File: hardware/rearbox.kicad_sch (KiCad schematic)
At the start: 0 parts

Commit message: Add components
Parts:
- added C1, C4, C5, C6, C7, C8: 100n, Capacitor_SMD:C_0603_1608Metric, symbol Device:C_Small
- added C2, C3: 10p, Capacitor_SMD:C_0603_1608Metric, symbol Device:C_Small
- added C?: 1u, Capacitor_SMD:C_0402_1005Metric_Pad0.74x0.62mm_HandSolder, symbol Device:C_Small
- added C?: 100n, Capacitor_SMD:C_0402_1005Metric_Pad0.74x0.62mm_HandSolder, symbol Device:C_Small
- added J1: Conn_01x06, Connector_PinHeader_2.54mm:PinHeader_1x06_P2.54mm_Vertical, symbol Connector_Generic:Conn_01x06
- added R1: 1k, Resistor_SMD:R_0402_1005Metric, symbol Device:R_Small
- added R2: 10k, Resistor_SMD:R_0402_1005Metric, symbol Device:R_Small
- added SW1: Tactswitch, Button_Switch_SMD:SW_SPST_B3U-1000P, symbol Switch:SW_Push
- added U1: STM32G473RCTx, Package_QFP:LQFP-64_10x10mm_P0.5mm, symbol MCU_ST_STM32G4:STM32G473RCTx
- added Y1: ABM8G-48.000MHZ, Crystal:Crystal_SMD_Abracon_ABM8G-4Pin_3.2x2.5mm, symbol Device:Crystal_GND24_Small
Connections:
- new net: R1.2, SW1.2
- new net +3.3VA: C?.1, C?.1, U1.29 (VDDA)
- new net +3V3: C1.1, C4.1, C6.1, C7.1, C8.1, J1.1 (Pin_1), R2.1, U1.1 (VBAT), U1.16 (VDD), U1.32 (VDD), U1.48 (VDD), U1.64 (VDD)
- new net ANALOG_INPUT1: U1.34 (PB12)
- new net ANALOG_INPUT2: U1.35 (PB13)
- new net ANALOG_INPUT3: U1.36 (PB14)
- new net ANALOG_INPUT4: U1.37 (PB15)
- new net ASSI_LED_BLUE: U1.3 (PC14)
- new net ASSI_LED_BUZZER: U1.4 (PC15)
- new net ASSI_LED_GREEN: U1.2 (PC13)
- new net ASSI_LED_RED: U1.54 (PC12)
- new net BRAKE_LIGHT: U1.24 (PB0)
- new net CAN2_RX: U1.61 (PB8)
- new net CAN2_TX: U1.62 (PB9)
- new net CAN_RX: U1.58 (PB5)
- new net CAN_TX: U1.59 (PB6)
- new net FAN_L: U1.25 (PB1)
- new net FAN_R: U1.26 (PB2)
- new net GND: C1.2, C2.2, C3.2, C4.2, C5.2, C6.2, C7.2, C8.2, C?.2, C?.2, J1.3 (Pin_3), SW1.1, U1.15 (VSS), U1.27 (VSSA), U1.31 (VSS), U1.47 (VSS), U1.63 (VSS), Y1.2, Y1.4
- new net HSE_IN: C2.1, U1.5 (PF0), Y1.1
- new net HSE_OUT: C3.1, U1.6 (PF1), Y1.3
- new net I^{2}C_SCL: U1.40 (PC8)
- new net I^{2}C_SDA: U1.41 (PC9)
- new net LED_CAN: U1.42 (PA8)
- new net LED_ERROR: U1.43 (PA9)
- new net LED_FUSE1: U1.44 (PA10)
- new net LED_FUSE2: U1.51 (PA15)
- new net LED_FUSE3: U1.60 (PB7)
- new net LED_FUSE4: U1.33 (PB11)
- new net MONO_TEMPERATURE: U1.10 (PC2)
- new net NRST: C5.1, J1.5 (Pin_5), R1.1, R2.2, U1.7 (PG10)
- new net PUMP_L: U1.56 (PB3)
- new net PUMP_R: U1.57 (PB4)
- new net RTDS_IN: U1.30 (PB10)
- new net SPI_MISO: U1.20 (PA6)
- new net SPI_MOSI: U1.21 (PA7)
- new net SPI_SCLK: U1.19 (PA5)
- new net SUSPENSION_POT1: U1.12 (PA0)
- new net SUSPENSION_POT2: U1.13 (PA1)
- new net SWCLK: J1.2 (Pin_2), U1.50 (PA14)
- new net SWDIO: J1.4 (Pin_4), U1.49 (PA13)
- new net UART_RX: U1.53 (PC11)
- new net UART_TX: U1.52 (PC10)
- new net USB_D+: U1.46 (PA12)
- new net USB_D-: U1.45 (PA11)
- new net WATER_PRESSURE1: U1.38 (PC6)
- new net WATER_PRESSURE2: U1.39 (PC7)
- new net WATER_TEMPERATURE1: U1.8 (PC0)
- new net WATER_TEMPERATURE2: U1.9 (PC1)
- new net ~{SPI_SS1}: U1.22 (PC4)
- new net ~{SPI_SS2}: U1.17 (PA3)
- new net ~{SPI_SS3}: U1.18 (PA4)
- no-connect marks 0 -> 2
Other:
- added sheet ASSI (assi.kicad_sch)
- added sheet Analog Inputs (analog_inputs.kicad_sch)
- added sheet Autosport (autosport.kicad_sch)
- added sheet Brake Light (brake_light.kicad_sch)
- added sheet CAN Transceivers (can_transceivers.kicad_sch)
- added sheet Fans (fans.kicad_sch)
- added sheet LEDs (leds.kicad_sch)
- added sheet Power Supply (power_supply.kicad_sch)
- added sheet Pumps (pumps.kicad_sch)
- added sheet RTDS (ready_to_drive_sound.kicad_sch)
- added sheet Safety Inputs (safety_inputs.kicad_sch)
- added sheet Suspension Potentiometers (suspension_potentiometers.kicad_sch)
- added sheet Temperature Sensors (temperature_sensors.kicad_sch)
- added sheet USB (usb.kicad_sch)
- added sheet Water Pressure Sensors (water_pressure_sensors.kicad_sch)
- note added: "GND"
- note added: "NRST"
- note added: "SWCLK"
- note added: "SWDIO"
- note added: "SWO"
- note added: "VDD"
- company: Author: I.Kajdan -> Author: I. Kajdan

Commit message: Add the Cube project
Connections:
- net ASSI_LED_RED is gone; now on net SPI_MOSI: U1.54 (PC12)
- net RTDS_IN is gone; now on net PUMP_R: U1.30 (PB10)
- net ~{SPI_SS1} is gone; now on net ANALOG_INPUT3: U1.22 (PC4)
- net ANALOG_INPUT1: now also U1.20 (PA6); no longer U1.34 (PB12)
- net ANALOG_INPUT2: now also U1.21 (PA7); no longer U1.35 (PB13)
- net ANALOG_INPUT3: no longer U1.36 (PB14)
- net ANALOG_INPUT4: now also U1.23 (PC5); no longer U1.37 (PB15)
- net BRAKE_LIGHT: now also U1.25 (PB1); no longer U1.24 (PB0)
- net CAN2_RX: now also U1.58 (PB5); no longer U1.61 (PB8)
- net CAN2_TX: now also U1.59 (PB6); no longer U1.62 (PB9)
- net CAN_RX: now also U1.61 (PB8); no longer U1.58 (PB5)
- net CAN_TX: now also U1.62 (PB9); no longer U1.59 (PB6)
- net FAN_L: now also U1.37 (PB15); no longer U1.25 (PB1)
- net FAN_R: now also U1.36 (PB14); no longer U1.26 (PB2)
- net I^{2}C_SCL: now also U1.43 (PA9); no longer U1.40 (PC8)
- net I^{2}C_SDA: now also U1.42 (PA8); no longer U1.41 (PC9)
- net LED_CAN: no longer U1.42 (PA8)
- net LED_ERROR: no longer U1.43 (PA9)
- net PUMP_L: now also U1.35 (PB13); no longer U1.56 (PB3)
- net PUMP_R: no longer U1.57 (PB4)
- net SPI_MISO: now also U1.57 (PB4); no longer U1.20 (PA6)
- net SPI_MOSI: no longer U1.21 (PA7)
- net SPI_SCLK: now also U1.56 (PB3); no longer U1.19 (PA5)
- net SUSPENSION_POT1: now also U1.13 (PA1); no longer U1.12 (PA0)
- net SUSPENSION_POT2: now also U1.14 (PA2); no longer U1.13 (PA1)
- net WATER_PRESSURE1: now also U1.11 (PC3); no longer U1.38 (PC6)
- net WATER_PRESSURE2: now also U1.12 (PA0); no longer U1.39 (PC7)
- net +3V3 renamed +3.3V
- net ASSI_LED_BLUE renamed ASSI_LED_G
- net ASSI_LED_BUZZER renamed ASSI_LED_B
- net ASSI_LED_GREEN renamed ASSI_LED_R
- net LED_FUSE1: no longer names the net of U1.44 (PA10)
- net LED_FUSE2: no longer names the net of U1.51 (PA15)
- net LED_FUSE3: no longer names the net of U1.60 (PB7)
- net LED_FUSE4: no longer names the net of U1.33 (PB11)
- net ~{SPI_SS2} renamed ASSI_BUZZER
- net ~{SPI_SS3} renamed ANALOG_OFFSET1
- new net ANALOG_OFFSET2: U1.19 (PA5)
- new net BUZZER: U1.26 (PB2)
- new net RTDS: U1.24 (PB0)
- new net SAFETY_SCL: U1.40 (PC8)
- new net SAFETY_SDA: U1.41 (PC9)
- new net SAFETY_~{INT}: U1.39 (PC7)
- new net SAFETY_~{RESET}: U1.38 (PC6)
- no-connect marks 2 -> 8
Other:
- sheet LEDs renamed LEDs & Buzzer
- sheet ASSI ports: added IN_BUZZER, OUT_BUZZER; removed IN_BUZZ, OUT_BUZZ
- sheet Analog Inputs ports: added REF1, REF2; removed none
- sheet LEDs & Buzzer ports: added BUZZER, FUSE, SAFETY; removed FUSE1, FUSE2, FUSE3, FUSE4
- sheet Safety Inputs ports: added IN_WHEEL_FL, IN_WHEEL_FR, IN_WHEEL_RL, IN_WHEEL_RR, LED_CAN, LED_ERROR, LED_FUSE, LED_SAFETY, SCL, SDA, ~{INT}, ~{RESET}; removed IN_W_FL, IN_W_FR, IN_W_RL, IN_W_RR, OUT_ASMS, OUT_FW, OUT_HV, OUT_HVD, OUT_INV, OUT_RES, OUT_RFU1, OUT_RFU2, OUT_W_FL, OUT_W_FR, OUT_W_RL, OUT_W_RR
- sheet Suspension Potentiometers ports: added IN_L, IN_R, OUT_L, OUT_R; removed IN1, IN2, OUT1, OUT2
- moved on the sheet: U1

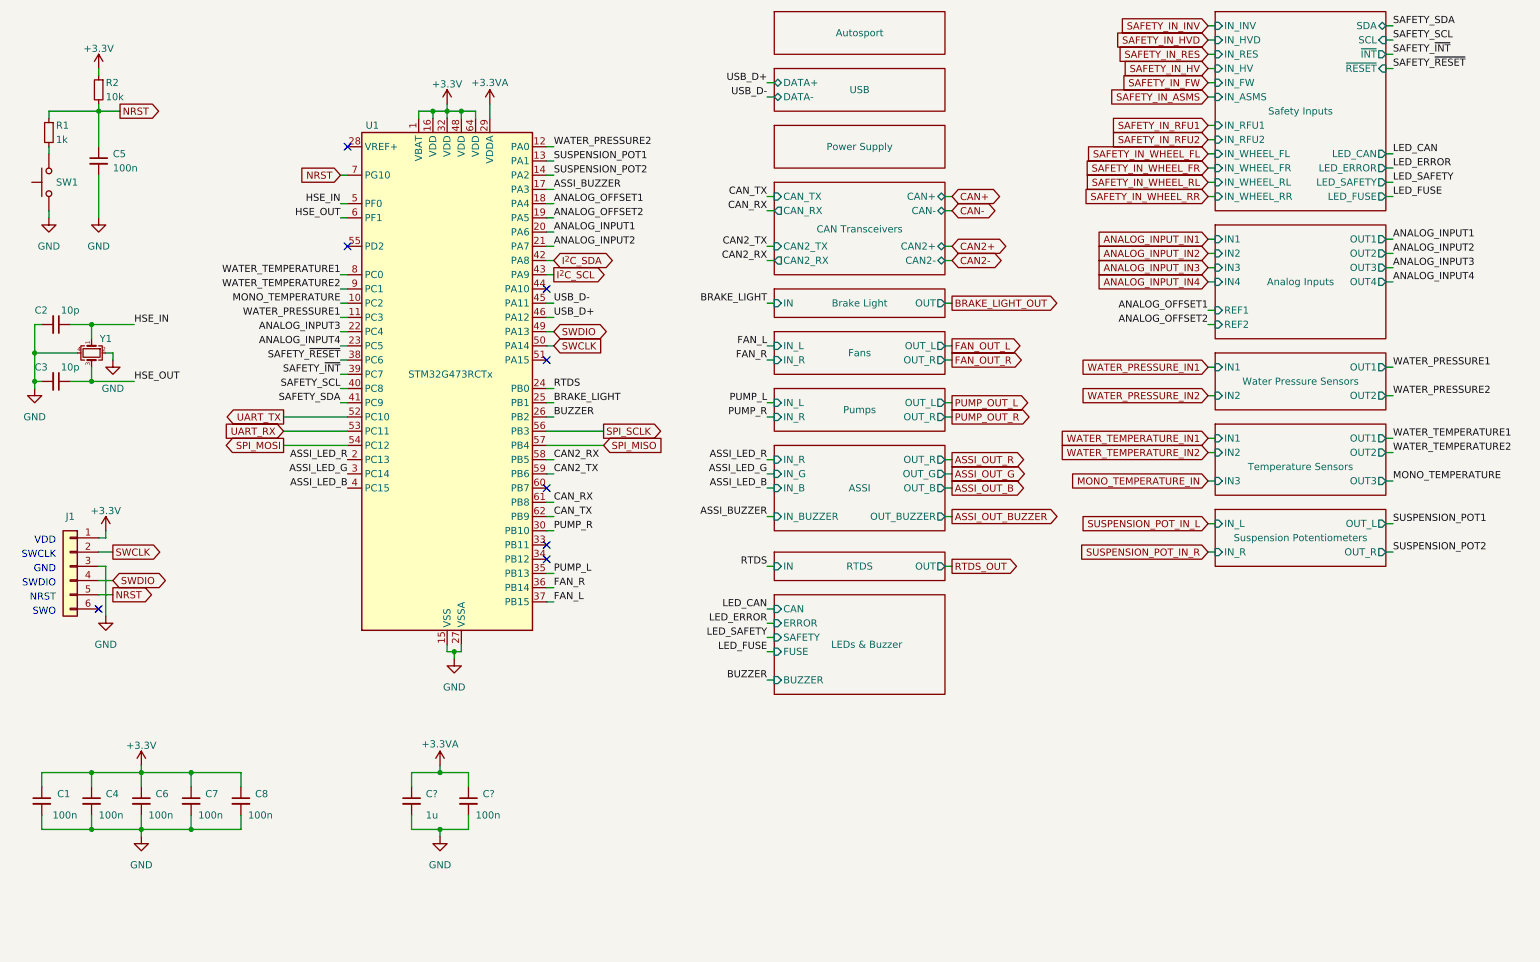
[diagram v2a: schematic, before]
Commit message: Improve the schematic
- add anti-aliasing filters
- rearrange the main connector signals
- improve the power filtering
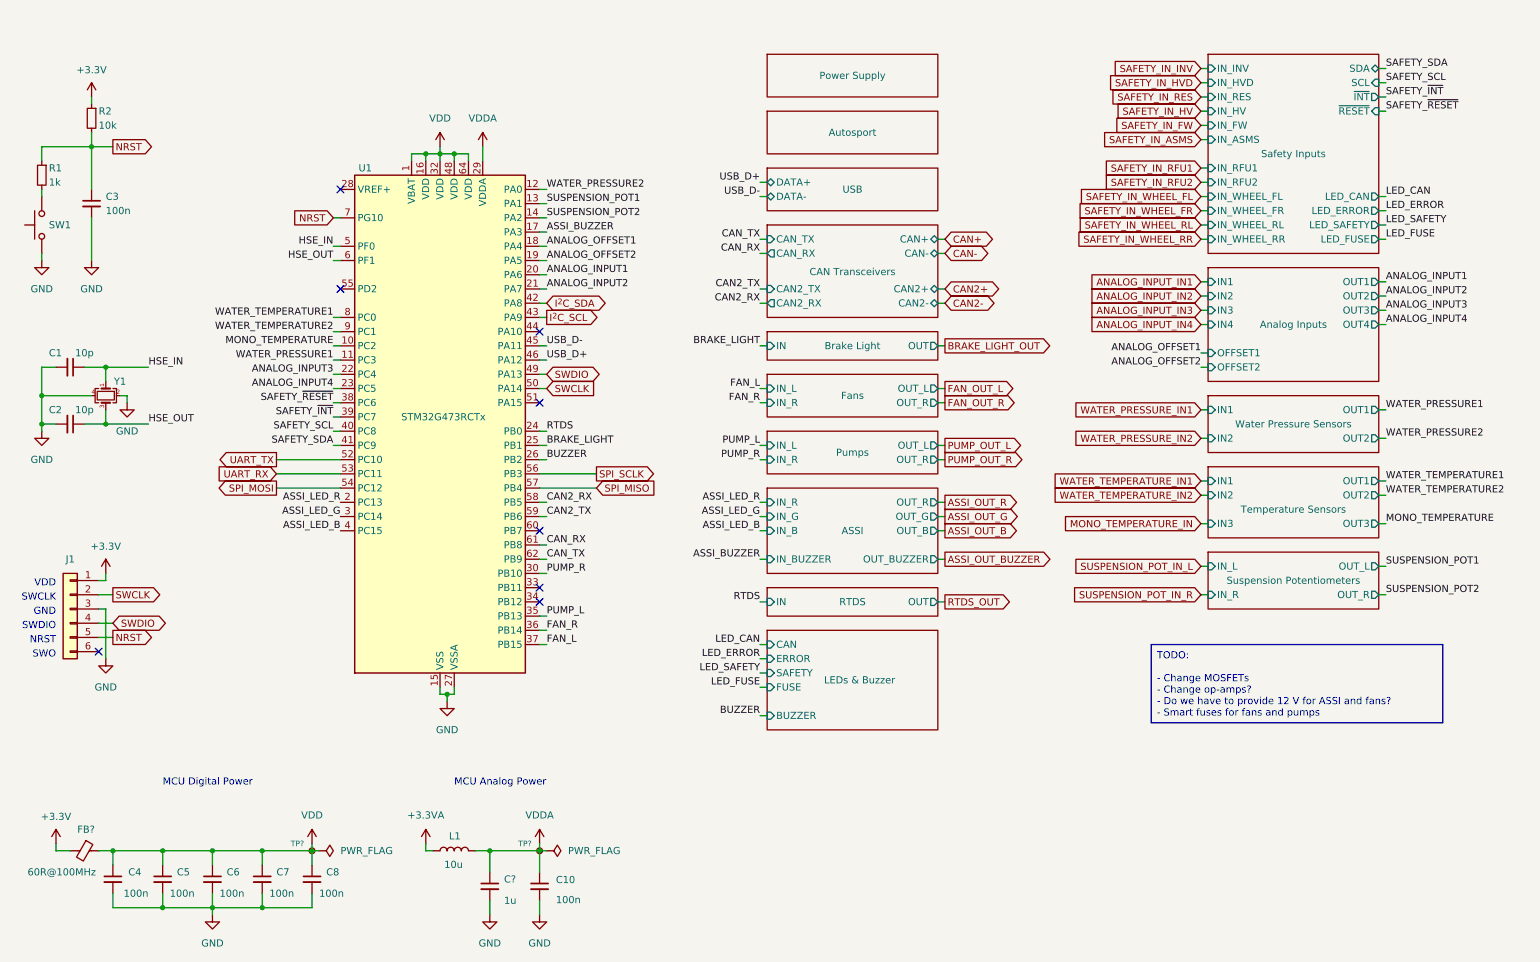
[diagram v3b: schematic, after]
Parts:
- removed C?: 100n, Capacitor_SMD:C_0402_1005Metric_Pad0.74x0.62mm_HandSolder, symbol Device:C_Small
- added C10: 100n, Capacitor_SMD:C_0603_1608Metric_Pad1.08x0.95mm_HandSolder, symbol Device:C_Small
- added FB?: 60R@100MHz, Inductor_SMD:L_0603_1608Metric, symbol Device:FerriteBead_Small
- added L1: 10u, Inductor_SMD:L_0603_1608Metric, symbol Device:L
- added TP? (x2): TestPoint_Small, TestPoint:TestPoint_Pad_D1.0mm, symbol Connector:TestPoint_Small
- C?: footprint Capacitor_SMD:C_0402_1005Metric_Pad0.74x0.62mm_HandSolder -> Capacitor_SMD:C_0603_1608Metric
- R1, R2: footprint Resistor_SMD:R_0402_1005Metric -> Resistor_SMD:R_0603_1608Metric
- renumbered C2 to C1, C3 to C2, C5 to C3, C1 to C4, C4 to C5
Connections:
- net +3.3V: now also FB?.2; no longer C4.1, C5.1, C6.1, C7.1, C8.1, U1.1 (VBAT), U1.16 (VDD), U1.32 (VDD), U1.48 (VDD), U1.64 (VDD)
- net +3.3VA: now also L1.1; no longer C?.1, U1.29 (VDDA)
- net GND: now also C10.2
- new net VDD: C4.1, C5.1, C6.1, C7.1, C8.1, FB?.1, TP?.1, U1.1 (VBAT), U1.16 (VDD), U1.32 (VDD), U1.48 (VDD), U1.64 (VDD)
- new net VDDA: C10.1, C?.1, L1.2, TP?.1, U1.29 (VDDA)
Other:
- sheet Analog Inputs ports: added OFFSET1, OFFSET2; removed REF1, REF2
- note added: "MCU Analog Power"
- note added: "MCU Digital Power"
- moved on the sheet: C1, C2, C3, C4, C5, C6, C7, C8, C?, J1, R1, R2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

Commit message: Set component values
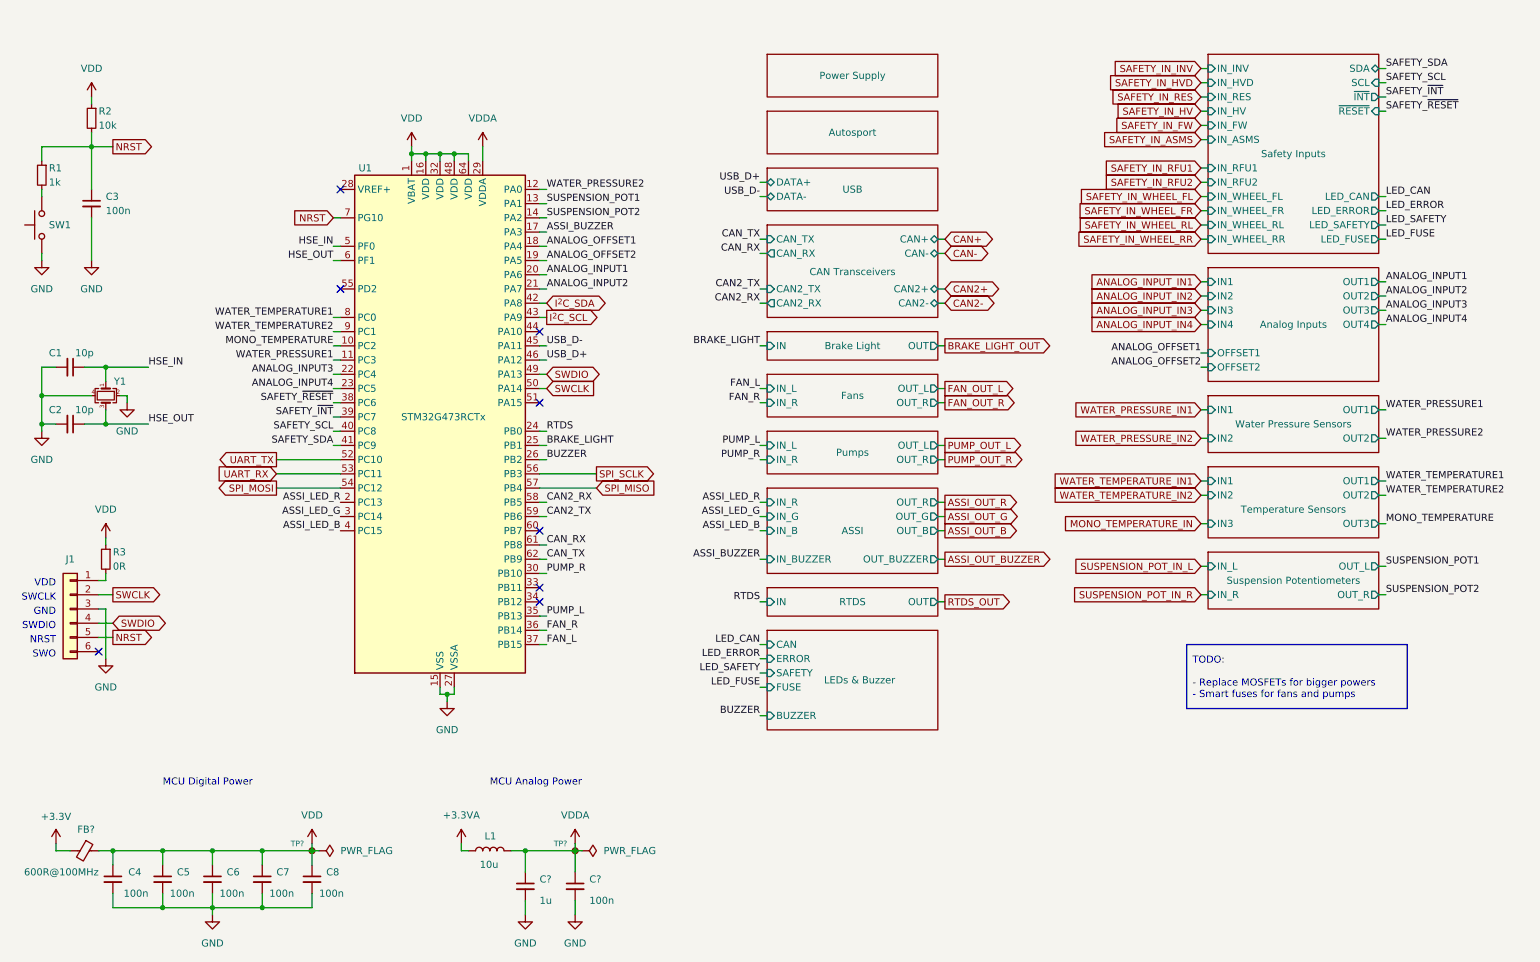
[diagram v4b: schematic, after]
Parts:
- removed C10: 100n, Capacitor_SMD:C_0603_1608Metric_Pad1.08x0.95mm_HandSolder, symbol Device:C_Small
- added C?: 100n, Capacitor_SMD:C_0603_1608Metric, symbol Device:C_Small
- added R3: 0R, Resistor_SMD:R_0603_1608Metric, symbol Device:R_Small
- FB?: value 60R@100MHz -> 600R@100MHz
- SW1: value Tactswitch -> Reset
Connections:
- net +3.3V: no longer J1.1 (Pin_1), R2.1
- net GND: now also C?.2
- net VDD: now also R2.1, R3.1
- net VDDA: now also C?.1
- new net: J1.1 (Pin_1), R3.2
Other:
- moved on the sheet: C?, L1, TP?
